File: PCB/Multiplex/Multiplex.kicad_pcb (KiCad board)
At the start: 2 copper layers, 48.3 x 40.6 mm, 16 parts, among them J1+1 Power, J1-1 Power, J2+1 I2C, J2-1 I2C, J3 Signal, J4 Track, U1 PIC16F1503-IP, U2 MOC3041M

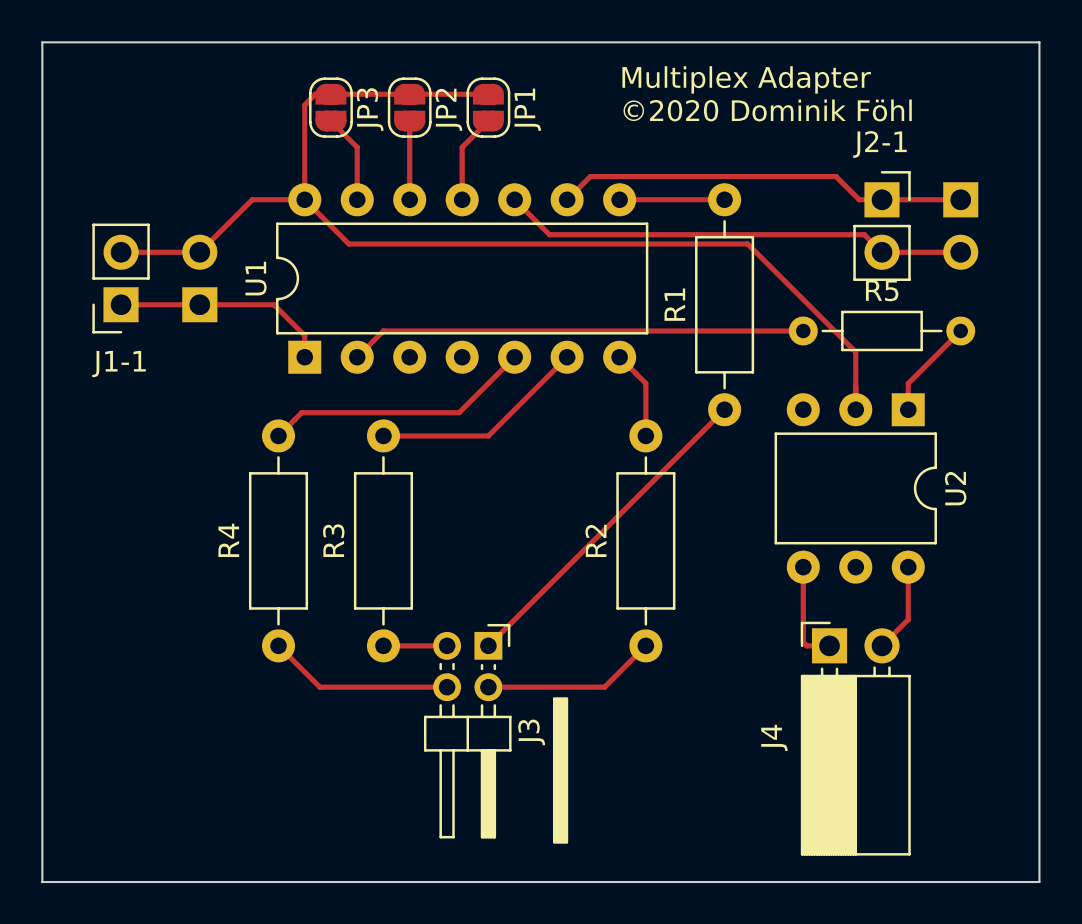
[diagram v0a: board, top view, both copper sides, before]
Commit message: .gitignore angepasst PCB Dateien hinzugefügt Can2Rest Webservice hinzugefügt
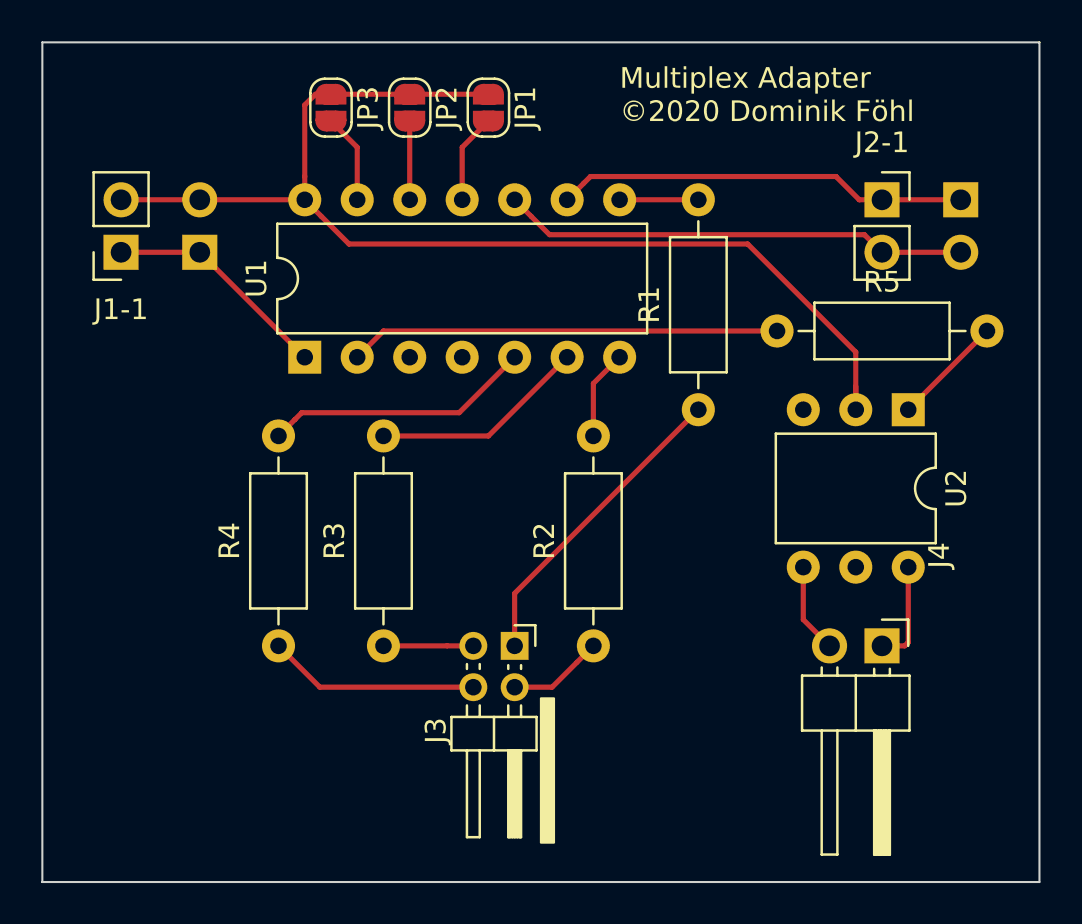
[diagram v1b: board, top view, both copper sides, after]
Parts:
- J4: footprint Connector_PinSocket_2.54mm:PinSocket_1x02_P2.54mm_Horizontal -> Connector_PinHeader_2.54mm:PinHeader_1x02_P2.54mm_Horizontal
- R5: footprint Resistor_THT:R_Axial_DIN0204_L3.6mm_D1.6mm_P7.62mm_Horizontal -> Resistor_THT:R_Axial_DIN0207_L6.3mm_D2.5mm_P10.16mm_Horizontal
- moved J4 2.54 mm to (177.8, 120.7), turned to 270 degrees
- moved J1+1 2.54 mm to (144.8, 101.6)
- moved J1-1 2.54 mm to (141.0, 101.6)
- moved R2 2.54 mm to (163.8, 120.7)
- moved J3 1.27 mm to (160.0, 120.7)
- moved R1 1.27 mm to (168.9, 109.2)
- moved R5 1.27 mm to (172.7, 105.4)
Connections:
- U2 pad 4: Net-(J4-Pad1) -> Net-(J4-Pad2)
- U2 pad 6: Net-(J4-Pad2) -> Net-(J4-Pad1)
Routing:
- net Net-(J3-Pad2): track 8.45 -> 4.64 mm
- net Net-(R5-Pad1): track 22.1 -> 20.8 mm
- net Net-(R1-Pad2): track 5.08 -> 3.81 mm
- net Net-(J3-Pad4): track 8.99 -> 10.3 mm
- net Net-(J3-Pad3): track 3.08 -> 4.35 mm
- net Net-(J3-Pad1): track 16.2 -> 15.1 mm
- net Net-(J1+1-Pad2): track 57.3 -> 56.2 mm
- net Net-(R5-Pad2): track 4.86 -> 5.39 mm

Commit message: Switch from MOC3041 to Relay.
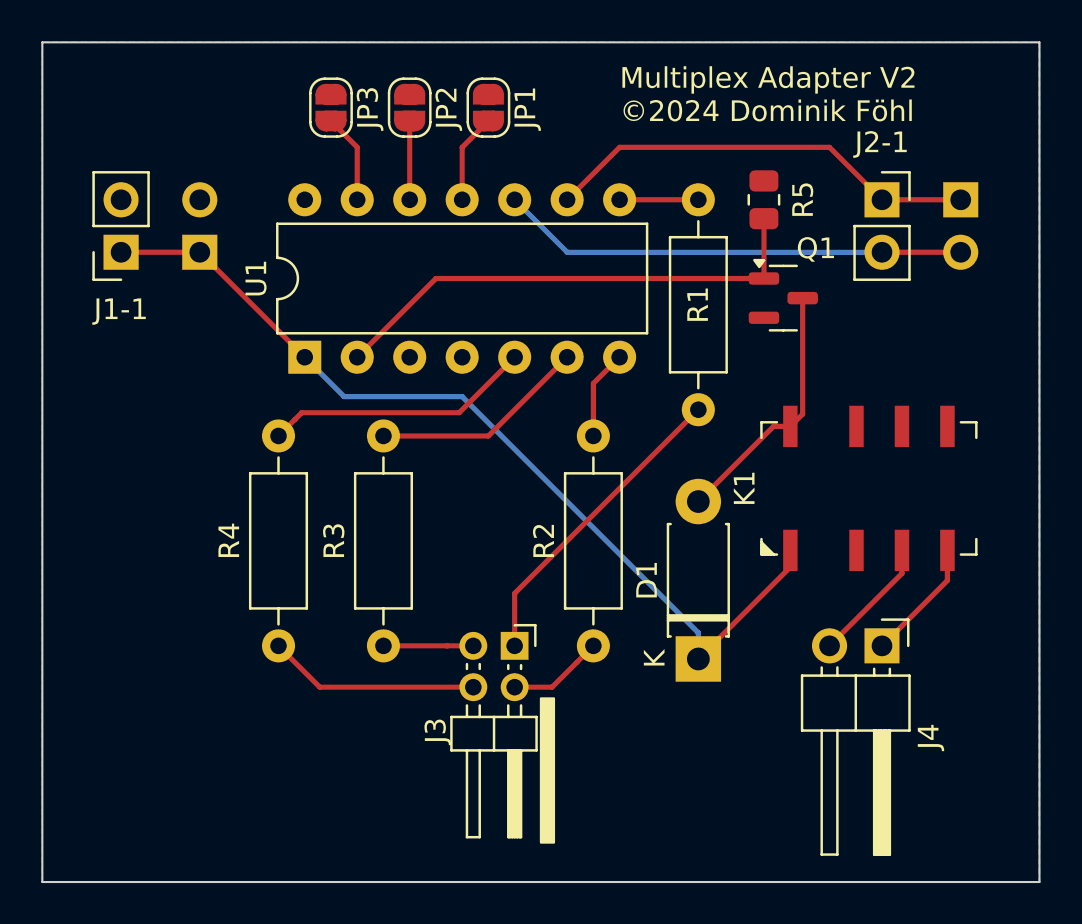
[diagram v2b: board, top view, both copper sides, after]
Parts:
- removed U2: MOC3041M, Package_DIP:DIP-6_W7.62mm
- added D1: D, Diode_THT:D_DO-41_SOD81_P7.62mm_Horizontal, F.Cu at (168.9, 121.3)
- added K1: IM03, Relay_SMD:Relay_2P2T_10x6mm_TE_IMxxG, F.Cu at (177.2, 113.0)
- added Q1: 2N7002, Package_TO_SOT_SMD:SOT-23, F.Cu at (173.0, 103.8)
- R5: value 150 -> 1M; footprint Resistor_THT:R_Axial_DIN0207_L6.3mm_D2.5mm_P10.16mm_Horizontal -> Resistor_SMD:R_0805_2012Metric
- moved R5 6.38 mm to (172.1, 99.1), turned to 90 degrees
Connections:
- net Net-(J1+1-Pad1) renamed +5V
- J1+1 pad 2: Net-(J1+1-Pad2) -> GND
- J1-1 pad 2: Net-(J1+1-Pad2) -> GND
- JP1 pad 1: Net-(J1+1-Pad2) -> GND
- JP2 pad 1: Net-(J1+1-Pad2) -> GND
- JP3 pad 1: Net-(J1+1-Pad2) -> GND
- R5 pad 2: Net-(R5-Pad2) -> GND
- U1 pad 14: Net-(J1+1-Pad2) -> GND
- U1 pad 3: Net-(U1-Pad3) -> unconnected-(U1-RA4/AN3/T1G/NCO1/SDO/CLKOUT-Pad3)
- U1 pad 4: Net-(U1-Pad4) -> unconnected-(U1-RA3/T1G/CLC1IN0/~{SS}/~{MCLR}/Vpp-Pad4)
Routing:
- net Net-(J1+1-Pad2): track 56.2 -> 0.00 mm
- net +5V: track 11.0 -> 43.9 mm
- net Net-(D1-A): track 0.00 -> 12.4 mm
- net Net-(R5-Pad2): track 5.39 -> 0.00 mm
- net Net-(Q1-G): track 20.8 -> 24.2 mm
- net Net-(J4-Pin_2): track 4.34 -> 6.07 mm
- net Net-(J2+1-Pin_1): track 20.0 -> 21.2 mm
- net Net-(J4-Pin_1): track 4.98 -> 5.93 mm
- added copper zone on B.Cu, net GND
- added copper zone on F.Cu, net GND
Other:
- net class Default removed
- board text added: "Multiplex Adapter V2 ©2024 Dominik Föhl"
- board text removed: "Multiplex Adapter ©2020 Dominik Föhl"

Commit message: Update PCBs and add track occupation PCB.
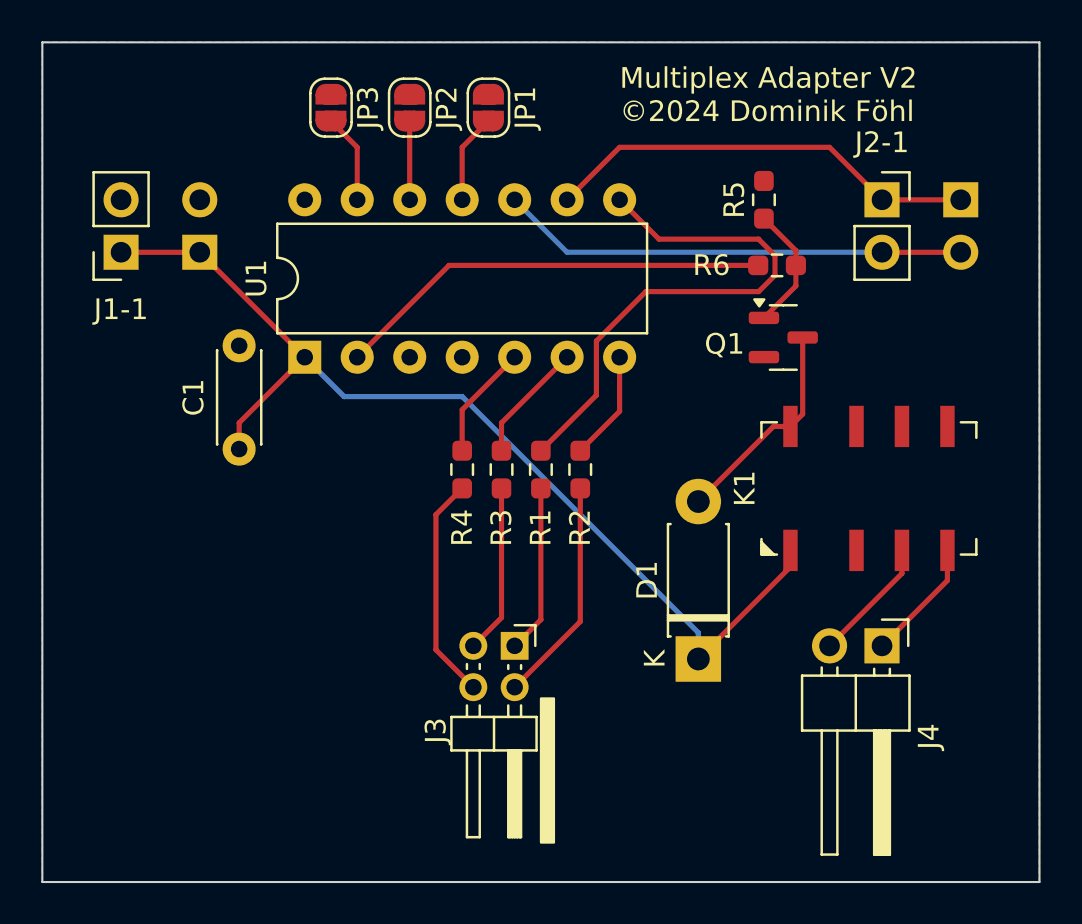
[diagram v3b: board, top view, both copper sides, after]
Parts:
- added C1: 470n, Capacitor_THT:C_Disc_D4.3mm_W1.9mm_P5.00mm, F.Cu at (146.7, 111.1)
- added R6: 0, Resistor_SMD:R_0603_1608Metric_Pad0.98x0.95mm_HandSolder, F.Cu at (172.7, 102.2)
- D1: value D -> 1N 4007-13
- R1, R2, R3, R4: footprint Resistor_THT:R_Axial_DIN0207_L6.3mm_D2.5mm_P10.16mm_Horizontal -> Resistor_SMD:R_0603_1608Metric_Pad0.98x0.95mm_HandSolder
- R5: value 1M -> 10k; footprint Resistor_SMD:R_0805_2012Metric -> Resistor_SMD:R_0603_1608Metric_Pad0.98x0.95mm_HandSolder
- moved R4 12.3 mm to (157.5, 112.1)
- moved R3 10.3 mm to (159.4, 112.1)
- moved R2 8.56 mm to (163.2, 112.1)
- moved R1 8.15 mm to (161.3, 112.1)
- moved Q1 1.91 mm to (173.0, 105.7)
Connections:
- U1 pad 2: Net-(Q1-G) -> Net-(U1-RA5/T1CKI/NCO1CLK/CLCIN1/CLKIN)
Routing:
- net Net-(U1-SDO/C2IN2-/C1IN2-/AN6/RC2): track 3.81 -> 26.0 mm
- net Net-(U1-RA5/T1CKI/NCO1CLK/CLCIN1/CLKIN): track 0.00 -> 21.2 mm
- net Net-(Q1-G): track 24.2 -> 6.08 mm
- net Net-(U1-PWM1/CLC1/CWG1A/RC5): track 13.0 -> 5.58 mm
- net Net-(J3-Pin_1): track 15.1 -> 8.15 mm
- net Net-(J3-Pin_2): track 4.64 -> 10.9 mm
- net +5V: track 43.9 -> 49.7 mm
- net Net-(U1-CLC2IN1/CWG1B/C2OUT/RC4): track 10.5 -> 5.84 mm
- net Net-(J3-Pin_3): track 4.35 -> 8.19 mm
- net Net-(D1-A): track 12.4 -> 10.5 mm
- net Net-(U1-~{SS}/PWM2/CLCIN0/C2IN3-/C1IN3-/AN7/RC3): track 4.34 -> 5.31 mm
- net Net-(J3-Pin_4): track 10.3 -> 10.9 mm

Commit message: Added new PCB and updated older ones.
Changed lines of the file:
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@@
 		)
 		(pad_to_mask_clearance 0.051)
-		(solder_mask_min_width 0.25)
 		(allow_soldermask_bridges_in_footprints no)
 		(pcbplotparams
@@
 	)
 	(segment
-		(start 180.965 117.485)
-		(end 177.8 120.65)
-		(width 0.25)
+		(start 177.8 120.65)
+		(end 180.965 117.485)
+		(width 1)
 		(layer "F.Cu")
 		(net 10)
 	)
 	(segment
-		(start 180.965 116.03)
-		(end 180.965 117.485)
-		(width 0.25)
+		(start 180.965 117.485)
+		(end 180.965 116.03)
+		(width 1)
 		(layer "F.Cu")
 		(net 10)
 	)
 	(segment
-		(start 178.765 117.145)
-		(end 175.26 120.65)
-		(width 0.25)
+		(start 175.26 120.65)
+		(end 175.26 120.09)
+		(width 1)
 		(layer "F.Cu")
 		(net 11)
 	)
 	(segment
-		(start 178.765 116.03)
-		(end 178.765 117.145)
-		(width 0.25)
+		(start 175.26 120.09)
+		(end 178.765 116.585)
+		(width 1)
+		(layer "F.Cu")
+		(net 11)
+	)
+	(segment
+		(start 178.765 116.585)
+		(end 178.765 116.03)
+		(width 1)
 		(layer "F.Cu")
 		(net 11)
